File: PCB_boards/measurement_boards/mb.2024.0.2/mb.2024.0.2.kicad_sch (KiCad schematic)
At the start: 27 parts, among them J1 DSP_out_12v_GND, J10 DSP+, J11 Screw_Terminal_VMN, J13 Connector_I2C_for_mux, J16 RX_bat, J17 DSP GND, J18 ELEC_M, J19 ELEC_N, J2 DPS5005_input_0_to_50V, J22 Conn_01x04_Female, J23 Conn_01x05_Female, J24 Connector_I2C_for_MC, J25 Conn_01x04_Female, J26 Conn_01x05_Female, J3 Screw_Terminal_AB, J4 Conn_01x08_Female, J5 Conn_01x04_Female, J6 Conn_01x08_Female, J7 Raspberry_Pi_2_3, J8 Connector_I2C_for_MCP23008, J9 TX_bat, U1 MCP23008-xP, U3 24LC02

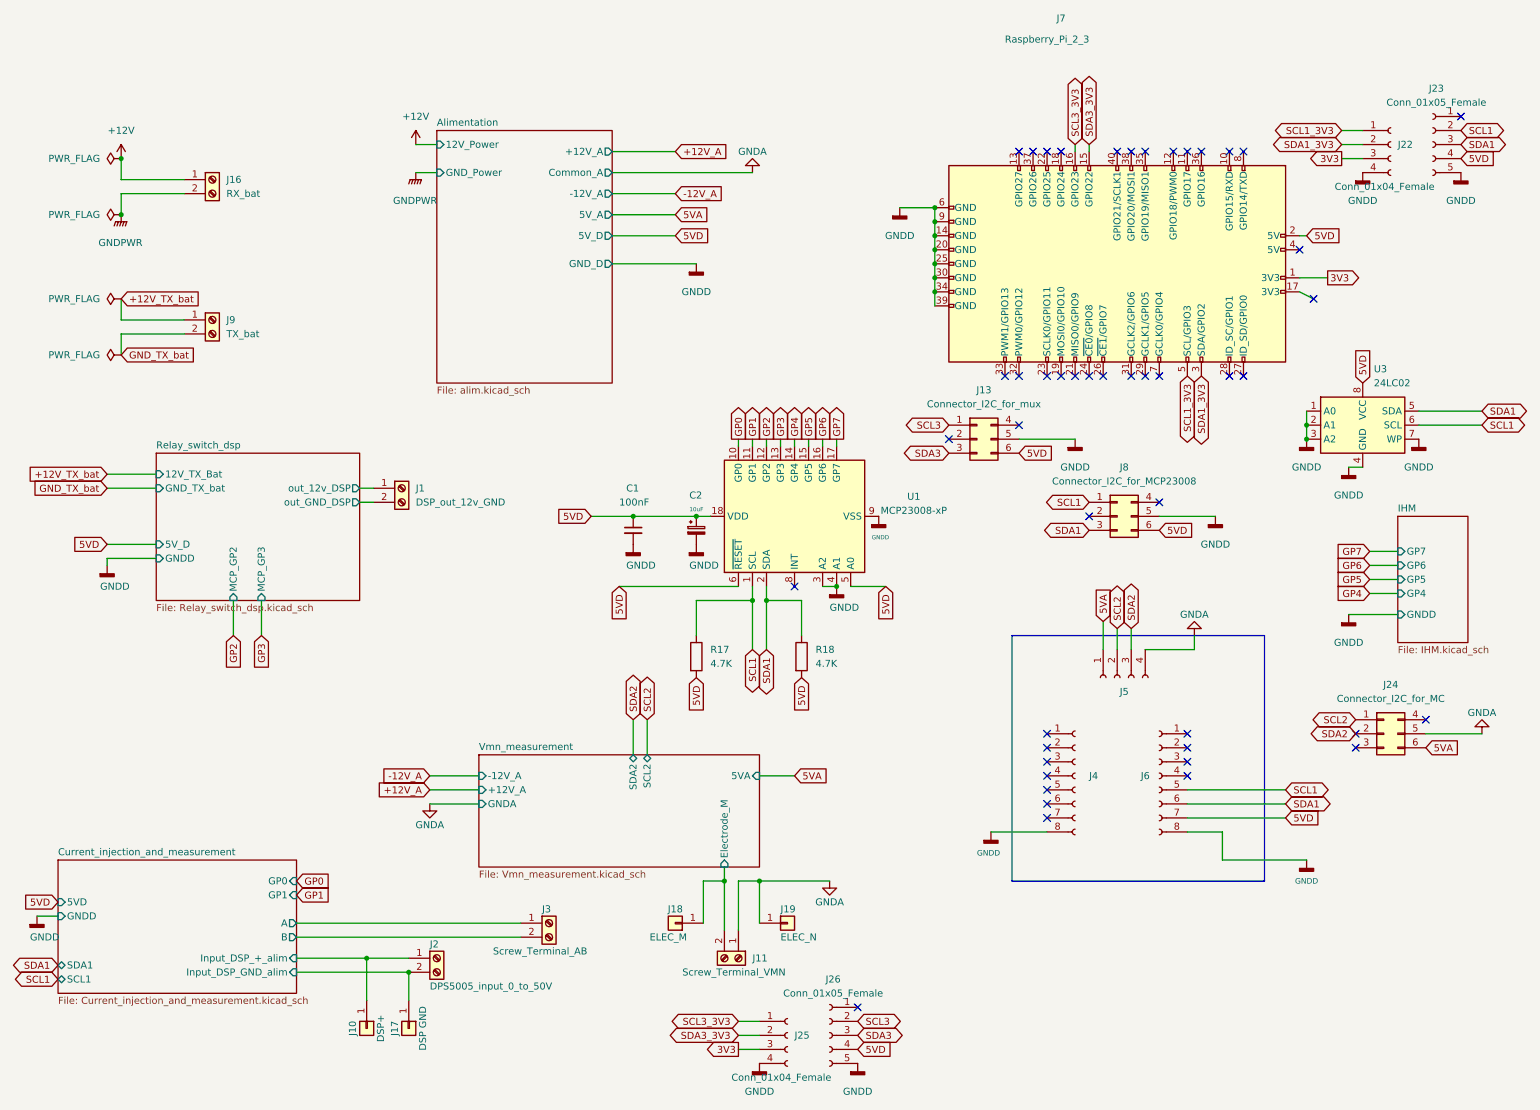
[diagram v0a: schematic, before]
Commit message: correction DPS, add dischage resistor, remove 63 warning on the schemtic, remove 7 errors in schematics change resistor designation, update pcb
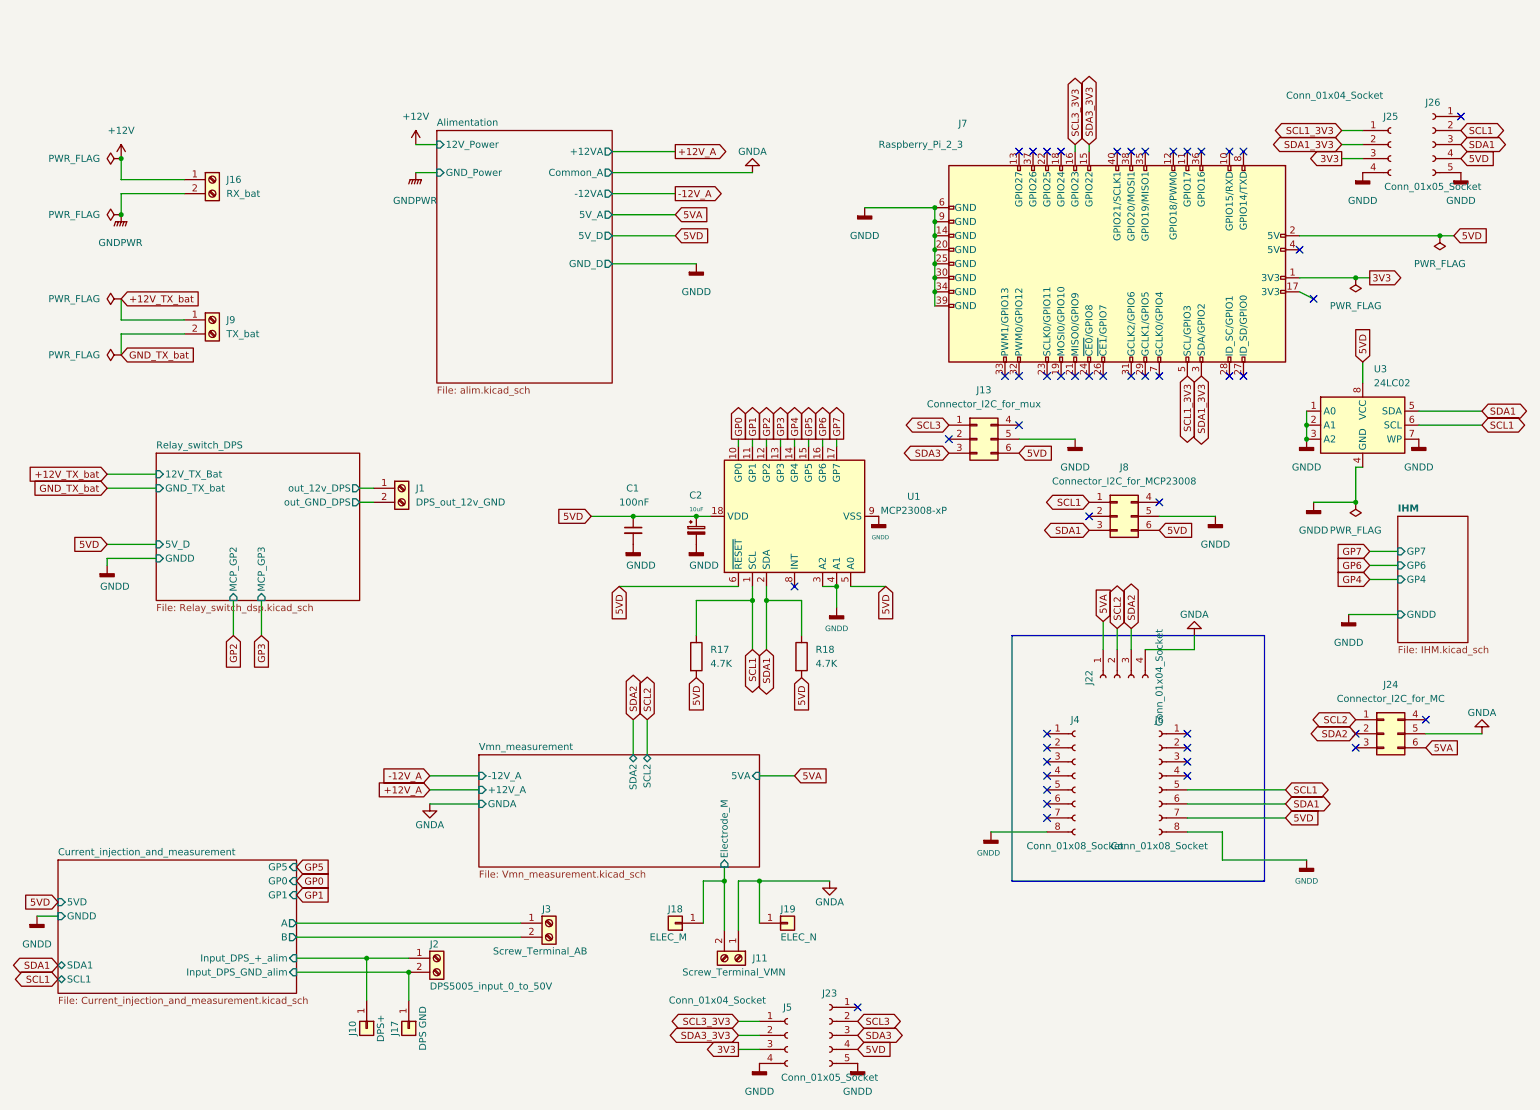
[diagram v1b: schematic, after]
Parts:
- J1: value DSP_out_12v_GND -> DPS_out_12v_GND
- J10: value DSP+ -> DPS+
- J17: value DSP GND -> DPS GND
- J22: renamed from J5; value Conn_01x04_Female -> Conn_01x04_Socket; symbol Connector:Conn_01x04_Female -> Connector:Conn_01x04_Socket
- J23: renamed from J26; value Conn_01x05_Female -> Conn_01x05_Socket; symbol Connector:Conn_01x05_Female -> Connector:Conn_01x05_Socket
- J25: renamed from J22; value Conn_01x04_Female -> Conn_01x04_Socket; symbol Connector:Conn_01x04_Female -> Connector:Conn_01x04_Socket
- J26: renamed from J23; value Conn_01x05_Female -> Conn_01x05_Socket; symbol Connector:Conn_01x05_Female -> Connector:Conn_01x05_Socket
- J4, J6: value Conn_01x08_Female -> Conn_01x08_Socket; symbol Connector:Conn_01x08_Female -> Connector:Conn_01x08_Socket
- J5: renamed from J25; value Conn_01x04_Female -> Conn_01x04_Socket; symbol Connector:Conn_01x04_Female -> Connector:Conn_01x04_Socket; now in the parts list
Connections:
- net Current_injection_and_measurement/Input_DSP_+_alim renamed Current_injection_and_measurement/Input_DPS_+_alim
- net Current_injection_and_measurement/Input_DSP_GND_alim renamed Current_injection_and_measurement/Input_DPS_GND_alim
- net Relay_switch_DPS/out_12v_DSP renamed Relay_switch_DPS/out_12v_DPS
- net Relay_switch_DPS/out_GND_DSP renamed Relay_switch_DPS/out_GND_DPS
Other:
- sheet Relay_switch_dsp renamed Relay_switch_DPS
- sheet Alimentation ports: added +12VA, -12VA; removed +12V_A, -12V_A
- sheet Current_injection_and_measurement ports: added GP5, Input_DPS_+_alim, Input_DPS_GND_alim; removed Input_DSP_+_alim, Input_DSP_GND_alim
- sheet IHM ports: added none; removed GP5
- sheet Relay_switch_DPS ports: added out_12v_DPS, out_GND_DPS; removed out_12v_DSP, out_GND_DSP
